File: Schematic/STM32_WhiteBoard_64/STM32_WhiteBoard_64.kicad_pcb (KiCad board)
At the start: 2 copper layers, 25.6 x 65 mm, 57 parts, among them J1 SWDIO+Serial, J2 USB_B_Micro, J3 Header1, J4 Header2, Q1 BC847BS, Q2 Si3493DDV, Q3 BC857BS, SW1 Boot0, SW2 Reset, U1 STM32F411RET6, U2 W25Q32JVSSIQ, U3 TPS3828-33DBVR, U4 TPS54302, X1 ASV-8MHz, Y1 ABS25-32.768KHZ-6-T

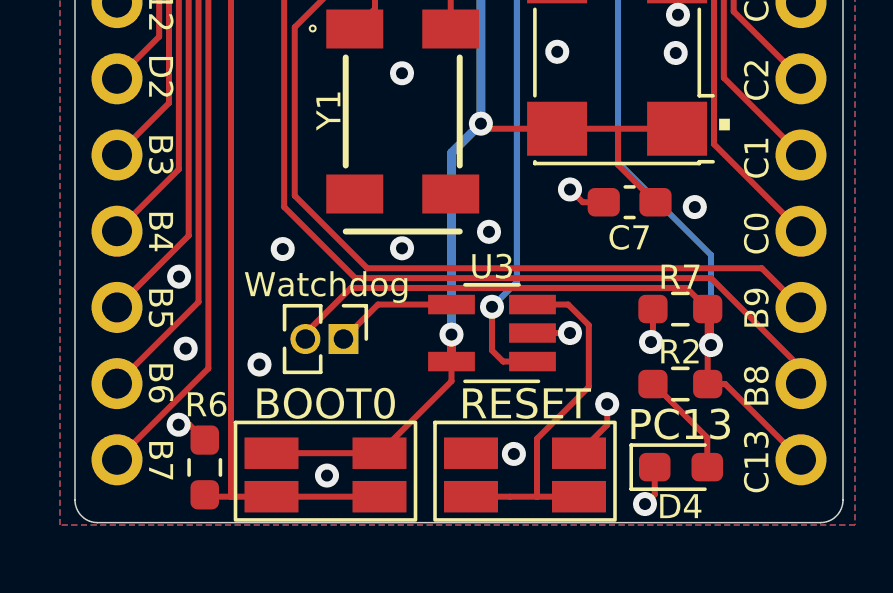
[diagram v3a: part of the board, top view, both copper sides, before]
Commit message: Added pull-up resistor for Reset
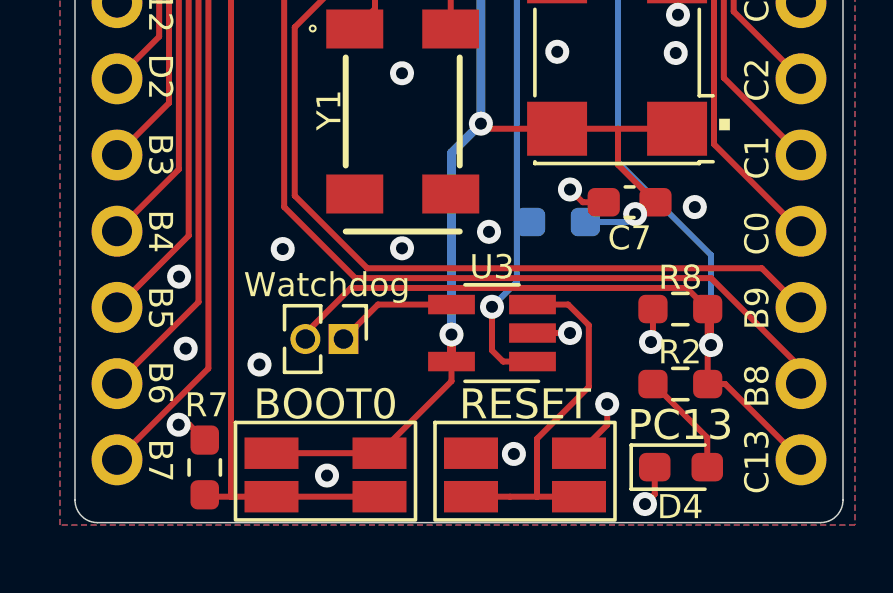
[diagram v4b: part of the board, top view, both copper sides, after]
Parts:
- added R5: 10kΩ, Resistor_SMD:R_0603_1608Metric_Pad0.98x0.95mm_HandSolder, B.Cu at (189.1, 133.4)
- C1: value 1µF -> 4.7µF
- renumbered R9 to R10, R10 to R11, R11 to R12, R12 to R13, R5 to R6, R6 to R7, R7 to R8, R8 to R9
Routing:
- net +3.3V: track 123.3 -> 125.9 mm, vias 9 -> 10
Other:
- board text added: "STM32_WhiteBoard_64 R0144B_Pb_2336 Bjørner Sandom"
- board text removed: "STM32_WhiteBoard_64 R0144_2334_Pb Bjørner Sandom"
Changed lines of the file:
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@@
     (property "ki_keywords" "R res resistor")
     (attr smd)
-    (fp_text reference "R6" (at -2.075 -0.061) (layer "F.SilkS")
+    (fp_text reference "R7" (at -2.075 -0.061) (layer "F.SilkS")
         (effects (font (size 0.8 0.8) (thickness 0.1)))
     )
@@
     (property "ki_keywords" "R res resistor")
     (attr smd)
-    (fp_text reference "R7" (at 0 -1.05 -360) (layer "F.SilkS")
+    (fp_text reference "R8" (at 0 -1.05 -360) (layer "F.SilkS")
         (effects (font (size 0.8 0.8) (thickness 0.1)))
     )
@@
       (net 57 "unconnected-(U1-OSC8M_OUT_(PD1)-Pad6)") (pinfunction "OSC8M_OUT_(PD1)") (pintype "input+no_connect"))
     (pad "7" smd roundrect locked (at -5.675 -0.75 135) (size 1.55 0.3) (layers "F.Cu" "F.Paste" "F.Mask") (roundrect_rratio 0.25)
-      (net 53 "/~{RESET}") (pinfunction "NRST") (pintype "input"))
+      (net 53 "/~{RESET}") (pinfunction "~{RESET}") (pintype "input"))
     (pad "8" smd roundrect locked (at -5.675 -0.25 135) (size 1.55 0.3) (layers "F.Cu" "F.Paste" "F.Mask") (roundrect_rratio 0.25)
       (net 18 "/PC0") (pinfunction "PC0-ADC") (pintype "bidirectional"))
@@
         (effects (font (size 0.8 0.8) (thickness 0.1)) (justify mirror))
     )
-    (fp_text value "1µF" (at 0 -1.43) (layer "B.Fab")
+    (fp_text value "4.7µF" (at 0 -1.43) (layer "B.Fab")
         (effects (font (size 1 1) (thickness 0.15)) (justify mirror))
     )
@@
     (property "ki_keywords" "R resistor")
     (attr smd)
-    (fp_text reference "R12" (at 0 1.43) (layer "B.SilkS")
+    (fp_text reference "R13" (at 0 1.43) (layer "B.SilkS")
         (effects (font (size 0.8 0.8) (thickness 0.1)) (justify mirror))
     )
@@
     )
   )
+  (footprint "Resistor_SMD:R_0603_1608Metric_Pad0.98x0.95mm_HandSolder" (layer "B.Cu")
+    (at 189.1 133.4)
+    (descr "Resistor SMD 0603 (1608 Metric), square (rectangular) end terminal, IPC_7351 nominal with elongated pad for handsoldering. (Body size source: IPC-SM-782 page 72, https://www.pcb-3d.com/wordpress/wp-content/uploads/ipc-sm-782a_amendment_1_and_2.pdf), generated with kicad-footprint-generator")
+    (tags "resistor handsolder")
+    (property "Sheetfile" "STM32_WhiteBoard_64.kicad_sch")
+    (property "Sheetname" "")
+    (property "ki_description" "Resistor")
+    (property "ki_keywords" "R res resistor")
+    (attr smd)
+    (fp_text reference "R5" (at 0 1.2) (layer "B.SilkS")
+        (effects (font (size 0.8 0.8) (thickness 0.1)) (justify mirror))
+    )
+    (fp_text value "10kΩ" (at 0 -1.43) (layer "B.Fab")
+        (effects (font (size 1 1) (thickness 0.15)) (justify mirror))
+    )
+    (fp_text user "${REFERENCE}" (at 0 0) (layer "B.Fab")
+        (effects (font (size 0.4 0.4) (thickness 0.06)) (justify mirror))
+    )
+    (fp_line (start -0.254724 -0.5225) (end 0.254724 -0.5225)
+      (stroke (width 0.12) (type solid)) (layer "B.SilkS"))
+    (fp_line (start -0.254724 0.5225) (end 0.254724 0.5225)
+      (stroke (width 0.12) (type solid)) (layer "B.SilkS"))
+    (fp_line (start -1.65 -0.73) (end -1.65 0.73)
+      (stroke (width 0.05) (type solid)) (layer "B.CrtYd"))
+    (fp_line (start -1.65 0.73) (end 1.65 0.73)
+      (stroke (width 0.05) (type solid)) (layer "B.CrtYd"))
+    (fp_line (start 1.65 -0.73) (end -1.65 -0.73)
+      (stroke (width 0.05) (type solid)) (layer "B.CrtYd"))
+    (fp_line (start 1.65 0.73) (end 1.65 -0.73)
+      (stroke (width 0.05) (type solid)) (layer "B.CrtYd"))
+    (fp_line (start -0.8 -0.4125) (end -0.8 0.4125)
+      (stroke (width 0.1) (type solid)) (layer "B.Fab"))
+    (fp_line (start -0.8 0.4125) (end 0.8 0.4125)
+      (stroke (width 0.1) (type solid)) (layer "B.Fab"))
+    (fp_line (start 0.8 -0.4125) (end -0.8 -0.4125)
+      (stroke (width 0.1) (type solid)) (layer "B.Fab"))
+    (fp_line (start 0.8 0.4125) (end 0.8 -0.4125)
+      (stroke (width 0.1) (type solid)) (layer "B.Fab"))
+    (pad "1" smd roundrect (at -0.9125 0) (size 0.975 0.95) (layers "B.Cu" "B.Paste" "B.Mask") (roundrect_rratio 0.25)
+      (net 53 "/~{RESET}") (pintype "passive"))
+    (pad "2" smd roundrect (at 0.9125 0) (size 0.975 0.95) (layers "B.Cu" "B.Paste" "B.Mask") (roundrect_rratio 0.25)
+      (net 44 "+3.3V") (pintype "passive"))
+    (model "${KICAD6_3DMODEL_DIR}/Resistor_SMD.3dshapes/R_0603_1608Metric.wrl"
+      (offset (xyz 0 0 0))
+      (scale (xyz 1 1 1))
+      (rotate (xyz 0 0 0))
+    )
+  )
   (footprint "Capacitor_SMD:C_0603_1608Metric_Pad1.08x0.95mm_HandSolder" (layer "B.Cu")
     (at 186.4 83.36 180)
@@
     (property "ki_keywords" "R resistor")
     (attr smd)
-    (fp_text reference "R10" (at 0 -1.15) (layer "B.SilkS")
+    (fp_text reference "R11" (at 0 -1.15) (layer "B.SilkS")
         (effects (font (size 0.8 0.8) (thickness 0.1)) (justify mirror))
     )
@@
     (property "ki_keywords" "R res resistor")
     (attr smd)
-    (fp_text reference "R5" (at 0.175 -1.11 180) (layer "B.SilkS")
+    (fp_text reference "R6" (at 0.175 -1.11 180) (layer "B.SilkS")
         (effects (font (size 0.8 0.8) (thickness 0.1)) (justify mirror))
     )
@@
     (property "ki_keywords" "R resistor")
     (attr smd)
-    (fp_text reference "R9" (at 0 1.13) (layer "B.SilkS")
+    (fp_text reference "R10" (at 0 1.13) (layer "B.SilkS")
         (effects (font (size 0.8 0.8) (thickness 0.1)) (justify mirror))
     )
@@
     (property "ki_keywords" "R resistor")
     (attr smd)
-    (fp_text reference "R11" (at 0 1.025) (layer "B.SilkS")
+    (fp_text reference "R12" (at 0 1.025) (layer "B.SilkS")
         (effects (font (size 0.8 0.8) (thickness 0.1)) (justify mirror))
     )
@@
     (property "ki_keywords" "R resistor")
     (attr smd)
-    (fp_text reference "R8" (at 0 -1.07) (layer "B.SilkS")
+    (fp_text reference "R9" (at 0 -1.07) (layer "B.SilkS")
         (effects (font (size 0.8 0.8) (thickness 0.1)) (justify mirror))
     )
@@
     (effects (font (size 1.5 1.5) (thickness 0.3) bold) (justify mirror))
   )
-  (gr_text "STM32_WhiteBoard_64\nR0144_2334_Pb\nBjørner Sandom\n" (at 180.462818 128.240001 90) (layer "B.SilkS")
+  (gr_text "STM32_WhiteBoard_64\nR0144B_Pb_2336\nBjørner Sandom\n" (at 180.462818 128.240001 90) (layer "B.SilkS")
     (effects (font (size 1 1) (thickness 0.15)) (justify mirror))
   )
@@
   (segment (start 191.1 130.29) (end 191.1 131.49) (width 0.2) (layer "F.Cu") (net 44))
   (segment (start 185.75 95.675) (end 185.75 97.55) (width 0.3) (layer "F.Cu") (net 44))
+  (segment (start 191.953099 133.136901) (end 192.35 132.74) (width 0.2) (layer "F.Cu") (net 44))
   (segment (start 189.07 130.29) (end 186.7 130.29) (width 0.2) (layer "F.Cu") (net 44))
   (segment (start 193.07 130.29) (end 191.1 130.29) (width 0.2) (layer "F.Cu") (net 44))
@@
   (segment (start 183.5 90.1) (end 182.27 91.33) (width 0.2) (layer "F.Cu") (net 44))
   (segment (start 181.7 114.19) (end 179.9867 114.19) (width 0.2) (layer "F.Cu") (net 44))
+  (segment (start 191.673209 133.136901) (end 191.953099 133.136901) (width 0.2) (layer "F.Cu") (net 44))
   (segment (start 182.27 91.33) (end 182.27 91.92) (width 0.2) (layer "F.Cu") (net 44))
   (segment (start 186.7 130.29) (end 186.53 130.12) (width 0.2) (layer "F.Cu") (net 44))
@@
   (via (at 186.53 130.12) (size 0.8) (drill 0.4) (layers "F.Cu" "B.Cu") (net 44))
   (via (at 183.87 90.1) (size 0.8) (drill 0.4) (layers "F.Cu" "B.Cu") (net 44))
+  (via (at 191.673209 133.136901) (size 0.8) (drill 0.4) (layers "F.Cu" "B.Cu") (net 44))
   (via (at 181.7 114.19) (size 0.8) (drill 0.4) (layers "F.Cu" "B.Cu") (net 44))
   (via (at 189.91875 115.10875) (size 0.8) (drill 0.4) (layers "F.Cu" "B.Cu") (net 44))
@@
   (segment (start 186.202312 121.394496) (end 186.608004 121.394496) (width 0.2) (layer "B.Cu") (net 44))
   (segment (start 187.1 115.53) (end 187.1 114.5375) (width 0.3) (layer "B.Cu") (net 44))
+  (segment (start 190.0125 133.4) (end 191.41011 133.4) (width 0.2) (layer "B.Cu") (net 44))
+  (segment (start 191.41011 133.4) (end 191.673209 133.136901) (width 0.2) (layer "B.Cu") (net 44))
   (segment (start 188.46 115.53) (end 187.1 115.53) (width 0.3) (layer "B.Cu") (net 44))
   (segment (start 188.465 115.525) (end 188.46 115.53) (width 0.3) (layer "B.Cu") (net 44))

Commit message: Basic IO tests
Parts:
- C1: value 4.7µF -> 10µF
- FB2: value FerriteBead_Small -> 100Ω@100MHz 30mΩ@DC
- R6: value 200Ω -> 270Ω
- R8: value 1MΩ -> 10kΩ
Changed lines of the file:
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@@
         (effects (font (size 0.8 0.8) (thickness 0.1)))
     )
-    (fp_text value "1MΩ" (at 0 1.43 -360) (layer "F.Fab")
+    (fp_text value "10kΩ" (at 0 1.43 -360) (layer "F.Fab")
         (effects (font (size 1 1) (thickness 0.15)))
     )
@@
         (effects (font (size 0.8 0.8) (thickness 0.1)) (justify mirror))
     )
-    (fp_text value "4.7µF" (at 0 -1.43) (layer "B.Fab")
+    (fp_text value "10µF" (at 0 -1.43) (layer "B.Fab")
         (effects (font (size 1 1) (thickness 0.15)) (justify mirror))
     )
@@
     (descr "Inductor SMD 0603 (1608 Metric), square (rectangular) end terminal, IPC_7351 nominal with elongated pad for handsoldering. (Body size source: http://www.tortai-tech.com/upload/download/2011102023233369053.pdf), generated with kicad-footprint-generator")
     (tags "inductor handsolder")
+    (property "Comments" "")
     (property "Sheetfile" "STM32_WhiteBoard_64.kicad_sch")
     (property "Sheetname" "")
@@
         (effects (font (size 0.8 0.8) (thickness 0.1)) (justify mirror))
     )
-    (fp_text value "FerriteBead_Small" (at 0 -1.43) (layer "B.Fab")
+    (fp_text value "100Ω@100MHz 30mΩ@DC" (at 0 -1.43) (layer "B.Fab")
         (effects (font (size 1 1) (thickness 0.15)) (justify mirror))
     )
@@
     (descr "TSOT26 AP62300")
     (tags "Integrated Circuit")
+    (property "Comments" "")
     (property "Sheetfile" "STM32_WhiteBoard_64.kicad_sch")
     (property "Sheetname" "")
@@
         (effects (font (size 0.8 0.8) (thickness 0.1)) (justify mirror))
     )
-    (fp_text value "200Ω" (at 0 -1.43) (layer "B.Fab")
-        (effects (font (size 1 1) (thickness 0.15)) (justify mirror))
-    )
+    (fp_text value "270Ω" (at 0 -1.43) (layer "B.Fab")
+        (effects (font (size 1 1) (thickness 0.15)) (justify mirror))
+    )

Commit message: Added voltage reference
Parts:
- added R1: 220Ω, Resistor_SMD:R_0603_1608Metric_Pad0.98x0.95mm_HandSolder, B.Cu at (192.4, 129.6)
- added R9: 100Ω, Resistor_SMD:R_0603_1608Metric_Pad0.98x0.95mm_HandSolder, B.Cu at (189.4, 133.9)
- added SW3: SW_DIP_x01, Retronics_Switches:CFS0102TA, F.Cu at (179.2, 132.6)
- added U1: LM4040DIM3X-2.0, Package_TO_SOT_SMD:SOT-23, B.Cu at (192.4, 126.7)
- C2: renamed from C3; value 10nF -> 100nF
- JP1: value WD_EN -> Jumper_3_Bridged12; footprint myDevices:PinHeader_1x02_P1.27mm_Vertical -> Connector_PinHeader_1.27mm:PinHeader_1x03_P1.27mm_Vertical
- L1: renamed from FB1; value 1kΩ@100MHz -> 22µH 2.4Ω
- R6: renamed from R5; moved to F.Cu
- U3: renamed from U2; footprint Package_SO:SOIC-8_3.9x4.9mm_P1.27mm -> Retronics_Memory:W25Q32JVSSIQ
- moved JP1 16.8 mm to (190.7, 123.0), turned to 90 degrees
- moved C7 1.88 mm to (192.9, 133.9)
- moved C9 1.10 mm to (192.0, 115.0)
- moved X1 0.64 mm to (191.1, 128.4)
- moved Y1 0.62 mm to (184.6, 129.7)
- moved R6 0.60 mm to (189.4, 133.9)
- moved C10 0.30 mm to (180.2, 115.0)
- moved D4 0.27 mm to (193.2, 141.3)
- moved G*** 0.11 mm to (177.0, 128.3)
- turned R8 to 90 degrees
- renumbered C2 to C3, FB2 to FB1, L1 to L2, R8 to R10, R9 to R11, R10 to R12, R11 to R13, R12 to R14, R13 to R15, R1 to R2, R2 to R3, R3 to R4, R4 to R5, R6 to R7, R7 to R8, U1 to U2, U3 to U4, U4 to U5
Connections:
- C1 pad 2: Net-(U1-VDDA) -> Net-(JP1-C)
- C2 pad 2: Net-(U1-VDDA) -> Net-(JP1-C)
- JP1 pad 2: /PC13 -> Net-(JP1-C)
- L1 pad 2: Net-(U1-VDDA) -> Net-(JP1-A)
- U2 pad 13: Net-(U1-VDDA) -> Net-(JP1-C)
- U4 pad 1: /~{RESET} -> Net-(U4-~{RESET})
- U4 pad 4: Net-(JP1-A) -> Net-(U4-WDI)
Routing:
- net Net-(JP1-B): track 0.00 -> 7.70 mm
- net Net-(U1-VDDA): track 7.60 -> 0.00 mm, vias 1 -> 0
- net Net-(JP1-C): track 0.00 -> 6.73 mm, vias 0 -> 1
- net Net-(U4-WDI): track 0.00 -> 6.55 mm
- net +3.3V: track 125.9 -> 132.4 mm
- net Net-(U4-~{RESET}): track 0.00 -> 5.67 mm, vias 0 -> 1
- net /PC13: track 41.4 -> 47.0 mm
- net /~{RESET}: track 47.8 -> 43.5 mm
- net /PA5: track 10.3 -> 12.1 mm
- net /PB9: track 31.6 -> 30.4 mm
- net /PA4: track 16.6 -> 17.7 mm
- net /PA6: track 16.7 -> 17.8 mm
- net /BOOT0: track 30.3 -> 29.6 mm
- net /PC0: track 17.7 -> 18.3 mm
- net GND: track 26.6 -> 27.2 mm, vias 75 -> 71
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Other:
- board text added: "2.048"
- board text added: "3.3"
- board text added: "STM32_WhiteBoard_64 R0144C_Pb_2339 Bjørner Sandom"
- board text added: "VREF"
- board text added: "Watch- dog"
- board text removed: "STM32_WhiteBoard_64 R0144B_Pb_2336 Bjørner Sandom"
- board text removed: "Watchdog"
